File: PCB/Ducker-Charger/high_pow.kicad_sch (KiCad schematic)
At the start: 37 parts, among them Q1 NCE3080K, Q2 NCE3080K, Q3 NCE3080K, Q4 NCE3080K, Q5 NCE3080K, U1 BQ25713RSNR, U2 TPS25750DRJKR

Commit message: fix: Rshunt
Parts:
- removed Q1, Q2, Q3, Q4, Q5: NCE3080K, EasyEDA:TO-252-2_L6.6-W6.1-P4.57-LS9.9-TL-CW, symbol EasyEDA:NCE3080K
- added Q15, Q16, Q17, Q18, Q19: BSC040N08NS5, EasyEDA:PG-TDSON-8_L5.9-W5.1-P1.27-LS6.2-BL, symbol EasyEDA:BSC040N08NS5
- L1: value 10u -> 2.2u
- R2, R3: value 10m -> 5m; footprint (none) -> EasyEDA:R3920
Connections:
- net +BATT: now also Q15.1 (S), Q15.2 (S), Q15.3 (S)
- net ACN: now also Q19.5 (D), Q19.6 (D), Q19.7 (D), Q19.8 (D)
- net GND: now also Q17.1 (S), Q17.2 (S), Q17.3 (S), Q18.1 (S), Q18.2 (S), Q18.3 (S)
- net SW1: now also Q18.5 (D), Q18.6 (D), Q18.7 (D), Q18.8 (D), Q19.1 (S), Q19.2 (S), Q19.3 (S)
- net SW2: now also Q16.1 (S), Q16.2 (S), Q16.3 (S), Q17.5 (D), Q17.6 (D), Q17.7 (D), Q17.8 (D)
- net V_SYS_A: now also Q16.5 (D), Q16.6 (D), Q16.7 (D), Q16.8 (D)
- net V_SYS_B: now also Q15.5 (D), Q15.6 (D), Q15.7 (D), Q15.8 (D)
- net ~{BATDRV}: now also Q15.4 (G)
- net at R4.2: now also Q17.4 (G)
- net at R6.2: now also Q16.4 (G)
- net at R5.2: now also Q18.4 (G)
- net at R1.2: now also Q19.4 (G)
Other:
- note added: "50V"
- note added: "I_sat>20A"
- note added: "NB: Rshunt is now half the Datasheet"
- note removed: "30V"
- moved on the sheet: C5, R1, R4, R5, R6

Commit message: feat: updated footprints
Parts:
- C1, C6: footprint (none) -> Capacitor_SMD:CP_Elec_10x10
- C10, C4, C5, C9: footprint (none) -> Capacitor_SMD:C_0603_1608Metric
- C11, C12, C13, C14, C15: footprint (none) -> Capacitor_SMD:C_0805_2012Metric
- C2, C3, C7, C8: footprint (none) -> Capacitor_SMD:C_2220_5750Metric
- L1: footprint (none) -> Inductor_SMD:L_12x12mm_H6mm
- R1, R10, R11, R4, R5, R6, R7, R8, R9: footprint (none) -> Resistor_SMD:R_0603_1608Metric
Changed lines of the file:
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@@
 			)
 		)
-		(property "Footprint" ""
+		(property "Footprint" "Inductor_SMD:L_12x12mm_H6mm"
 			(at 165.1 60.96 0)
 			(effects
@@
 			)
 		)
-		(property "Footprint" ""
+		(property "Footprint" "Capacitor_SMD:C_0805_2012Metric"
 			(at 180.0352 139.7 0)
 			(effects
@@
 			)
 		)
-		(property "Footprint" ""
+		(property "Footprint" "Capacitor_SMD:C_2220_5750Metric"
 			(at 133.0452 73.66 0)
 			(effects
@@
 			)
 		)
-		(property "Footprint" ""
+		(property "Footprint" "Resistor_SMD:R_0603_1608Metric"
 			(at 155.448 46.99 90)
 			(effects
@@
 			)
 		)
-		(property "Footprint" ""
+		(property "Footprint" "Capacitor_SMD:C_2220_5750Metric"
 			(at 207.9752 73.66 0)
 			(effects
@@
 			)
 		)
-		(property "Footprint" ""
+		(property "Footprint" "Capacitor_SMD:CP_Elec_10x10"
 			(at 194.0052 73.66 0)
 			(effects
@@
 			)
 		)
-		(property "Footprint" ""
+		(property "Footprint" "Resistor_SMD:R_0603_1608Metric"
 			(at 177.038 86.36 90)
 			(effects
@@
 			)
 		)
-		(property "Footprint" ""
+		(property "Footprint" "Capacitor_SMD:C_0805_2012Metric"
 			(at 201.6252 139.7 0)
 			(effects
@@
 			)
 		)
-		(property "Footprint" ""
+		(property "Footprint" "Capacitor_SMD:C_2220_5750Metric"
 			(at 201.6252 73.66 0)
 			(effects
@@
 			)
 		)
-		(property "Footprint" ""
+		(property "Footprint" "Resistor_SMD:R_0603_1608Metric"
 			(at 179.578 46.99 90)
 			(effects
@@
 			)
 		)
-		(property "Footprint" ""
+		(property "Footprint" "Resistor_SMD:R_0603_1608Metric"
 			(at 159.258 86.36 90)
 			(effects
@@
 			)
 		)
-		(property "Footprint" ""
+		(property "Footprint" "Resistor_SMD:R_0603_1608Metric"
 			(at 103.632 143.51 90)
 			(effects
@@
 			)
 		)
-		(property "Footprint" ""
+		(property "Footprint" "Capacitor_SMD:C_0603_1608Metric"
 			(at 171.1452 139.7 0)
 			(effects
@@
 			)
 		)
-		(property "Footprint" ""
+		(property "Footprint" "Resistor_SMD:R_0603_1608Metric"
 			(at 103.632 135.89 90)
 			(effects
@@
 			)
 		)
-		(property "Footprint" ""
+		(property "Footprint" "Capacitor_SMD:C_0805_2012Metric"
 			(at 51.7652 185.42 0)
 			(effects
@@
 			)
 		)
-		(property "Footprint" ""
+		(property "Footprint" "Capacitor_SMD:C_0603_1608Metric"
 			(at 160.3248 48.26 0)
 			(effects
@@
 			)
 		)
-		(property "Footprint" ""
+		(property "Footprint" "Capacitor_SMD:CP_Elec_10x10"
 			(at 125.4252 73.66 0)
 			(effects
@@
 			)
 		)
-		(property "Footprint" ""
+		(property "Footprint" "Capacitor_SMD:C_2220_5750Metric"
 			(at 139.3952 73.66 0)
 			(effects
@@
 			)
 		)
-		(property "Footprint" ""
+		(property "Footprint" "Capacitor_SMD:C_0603_1608Metric"
 			(at 169.8752 55.88 0)
 			(effects
@@
 			)
 		)
-		(property "Footprint" ""
+		(property "Footprint" "Resistor_SMD:R_0603_1608Metric"
 			(at 196.85 133.858 90)
 			(effects
@@
 			)
 		)
-		(property "Footprint" ""
+		(property "Footprint" "Resistor_SMD:R_0603_1608Metric"
 			(at 129.032 135.89 90)
 			(effects
@@
 			)
 		)
-		(property "Footprint" ""
+		(property "Footprint" "Capacitor_SMD:C_0603_1608Metric"
 			(at 162.2552 139.7 0)
 			(effects
@@
 			)
 		)
-		(property "Footprint" ""
+		(property "Footprint" "Resistor_SMD:R_0603_1608Metric"
 			(at 129.032 143.51 90)
 			(effects
@@
 			)
 		)
-		(property "Footprint" ""
+		(property "Footprint" "Capacitor_SMD:C_0805_2012Metric"
 			(at 37.7952 185.42 0)
 			(effects
@@
 			)
 		)
-		(property "Footprint" ""
+		(property "Footprint" "Capacitor_SMD:C_0805_2012Metric"
 			(at 25.0952 185.42 0)
 			(effects

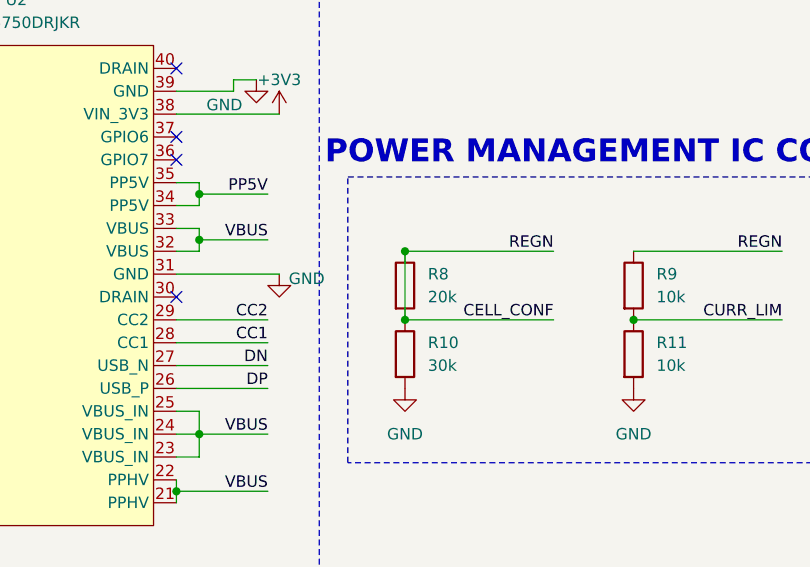
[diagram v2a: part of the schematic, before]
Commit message: fix: changed rshunt footprint
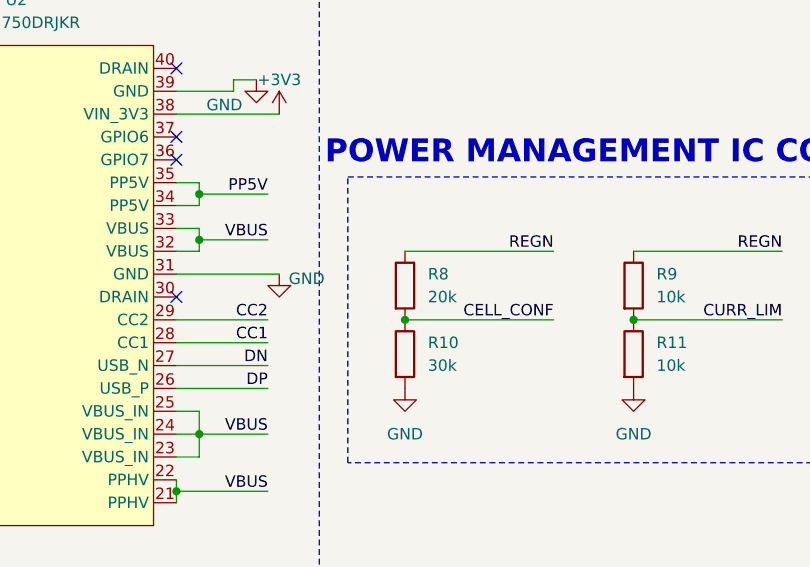
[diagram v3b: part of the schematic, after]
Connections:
- net CELL_CONF: no longer C11.1, R7.1, R8.1, R9.1, U1.28 (REGN)
- new net REGN: C11.1, R7.1, R8.1, R9.1, U1.28 (REGN)
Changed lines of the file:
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@@
-	)
-	(junction
-		(at 105.41 132.08)
-		(diameter 0)
-		(color 0 0 0 0)
 	)
 	(junction
@@
 		)
 		(stroke
-			(width 0)
-			(type default)
-		)
-	)
-	(wire
-		(pts
-			(xy 105.41 139.7) (xy 105.41 132.08)
-		)
-		(stroke

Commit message: fix: new BUCK-BOOST power stage
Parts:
- removed C10, C9: 100n, Capacitor_SMD:C_0603_1608Metric, symbol Device:C
- removed C11: 4.7u, Capacitor_SMD:C_0805_2012Metric, symbol Device:C
- removed C12: 1u, Capacitor_SMD:C_0805_2012Metric, symbol Device:C
- removed R10: 30k, Resistor_SMD:R_0603_1608Metric, symbol Device:R
- removed R11, R9: 10k, Resistor_SMD:R_0603_1608Metric, symbol Device:R
- removed R7: 10, Resistor_SMD:R_0603_1608Metric, symbol Device:R
- removed R8: 20k, Resistor_SMD:R_0603_1608Metric, symbol Device:R
- added C57, C77: 1u, symbol Device:C
- added C58, C59, C60, C61, C62, C63, C70, C71, C72, C73, C74, C75: 10u, symbol Device:C
- added C64: 470n, symbol Device:C
- added C65, C66: 33n, symbol Device:C
- added C67: 10n, symbol Device:C
- added C68, C69: 47n, symbol Device:C
- added C76: 0.1, symbol Device:C
- added L6: 2.2u, Inductor_SMD:L_12x12mm_H6mm, symbol Device:L
- added Q13, Q3, Q4, Q5: BSC040N08NS5, EasyEDA:PG-TDSON-8_L5.9-W5.1-P1.27-LS6.2-BL, symbol EasyEDA:BSC040N08NS5
- added Q14: PMOS, symbol Simulation_SPICE:PMOS
- added R58: 2.2, symbol Device:R
- added R59: 5m, EasyEDA:R3920, symbol Device:R
- added R60: 1, symbol Device:R
- added R61, R62: 4.99, symbol Device:R
- added R63: 10m, EasyEDA:R3920, symbol Device:R
- added R64, R65: 10, symbol Device:R
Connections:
- net +BATT: now also C76.1, R63.2, R65.1
- net ACN: now also C66.1, R62.2
- net ACP: now also C64.1, C65.1, R60.2, R61.2
- net BTST1: now also C68.2
- net BTST2: now also C69.2
- net GND: now also C57.2, C58.2, C59.2, C60.2, C61.2, C62.2, C63.2, C64.2, C65.2, C66.2, C67.2, C70.2, C71.2, C72.2, C73.2, C74.2, C75.2, C77.2, Q4.1 (S), Q4.2 (S), Q4.3 (S), Q5.1 (S), Q5.2 (S), Q5.3 (S)
- net HIDRV1: now also Q3.4 (G)
- net HIDRV2: now also Q13.4 (G)
- net LODRV1: now also Q4.4 (G)
- net LODRV2: now also Q5.4 (G)
- net SW1: now also C68.1, L6.1, Q3.1 (S), Q3.2 (S), Q3.3 (S), Q4.5 (D), Q4.6 (D), Q4.7 (D), Q4.8 (D)
- net SW2: now also C69.1, L6.2, Q13.5 (D), Q13.6 (D), Q13.7 (D), Q13.8 (D), Q5.5 (D), Q5.6 (D), Q5.7 (D), Q5.8 (D)
- net ~{BATDRV}: now also Q14.2 (G)
- new net: C76.2, C77.1, Q14.1 (D), R63.1, R64.1
- new net: C67.1, Q3.5 (D), Q3.6 (D), Q3.7 (D), Q3.8 (D), R59.2, R62.1
- new net: C57.1, R58.2
- new net ADAPTER: C58.1, C59.1, C60.1, C61.1, C62.1, C63.1, R58.1, R59.1, R60.1, R61.1
- new net SRN: R65.2
- new net SRP: R64.2
- new net SYS: C70.1, C71.1, C72.1, C73.1, C74.1, C75.1, Q13.1 (S), Q13.2 (S), Q13.3 (S), Q14.3 (S)
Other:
- note removed: "NB: Rshunt is now half the Datasheet"
- moved on the sheet: C1, C2, C3, C4, C5, C6, C7, C8, D2, D4, L1, Q15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

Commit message: fix: remade entire ICs configuration
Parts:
- removed C1: 220u, Capacitor_SMD:CP_Elec_10x10, symbol Device:C_Polarized
- removed C4, C5: 47n, Capacitor_SMD:C_0603_1608Metric, symbol Device:C
- removed D4: SMBJ22A-E3/52, EasyEDA:SMB_L4.3-W3.6-LS5.4-RD, symbol Device:D_Schottky
- removed L1: 2.2u, Inductor_SMD:L_12x12mm_H6mm, symbol Device:L
- removed Q14: PMOS, symbol Simulation_SPICE:PMOS
- removed Q15, Q16, Q17, Q18, Q19: BSC040N08NS5, EasyEDA:PG-TDSON-8_L5.9-W5.1-P1.27-LS6.2-BL, symbol EasyEDA:BSC040N08NS5
- removed R1, R4, R5, R6: 10, Resistor_SMD:R_0603_1608Metric, symbol Device:R
- removed R2, R3: 5m, EasyEDA:R3920, symbol Device:R
- added C1: 10u, symbol Device:C
- added C10: C, symbol Device:C
- added C11: 15p, symbol Device:C
- added C12: 1800p, symbol Device:C
- added C4, C5: 100u, symbol Device:C_Polarized
- added C78: 33p, symbol Device:C
- added C79: 680p, symbol Device:C
- added C80: 100p, symbol Device:C
- added C81: 10u, Capacitor_SMD:C_0603_1608Metric, symbol Device:C
- added C82: 330p, symbol Device:C
- added C9: 1u, symbol Device:C
- added D1: LED, LED_SMD:LED_0603_1608Metric, symbol Device:LED
- added Q15: SI7157DP-T1-GE3, EasyEDA:POWERPAK-SO-8_L5.9-W4.9-P1.27-LS6.2-BL, symbol EasyEDA:SI7157DP-T1-GE3
- added R10: 350k, Resistor_SMD:R_0603_1608Metric, symbol Device:R
- added R11: 250k, Resistor_SMD:R_0603_1608Metric, symbol Device:R
- added R66, R69, R74, R75: 10k, Resistor_SMD:R_0603_1608Metric, symbol Device:R
- added R67: 40.2k, Resistor_SMD:R_0603_1608Metric, symbol Device:R
- added R68: 137k, Resistor_SMD:R_0603_1608Metric, symbol Device:R
- added R7: 10, symbol Device:R
- added R70: 30k, Resistor_SMD:R_0603_1608Metric, symbol Device:R
- added R71: 100k, Resistor_SMD:R_0603_1608Metric, symbol Device:R
- added R72: 300k, Resistor_SMD:R_0603_1608Metric, symbol Device:R
- added R73: 1k, Resistor_SMD:R_0603_1608Metric, symbol Device:R
- added R8: 383k, Resistor_SMD:R_0603_1608Metric, symbol Device:R
- added R9: 220k, Resistor_SMD:R_0603_1608Metric, symbol Device:R
- C13, C14, C15: value 4.7u -> 10u
- C2, C3: footprint Capacitor_SMD:C_2220_5750Metric -> (none)
- C58, C59, C60, C61, C62, C63, C67, C70, C71, C72, C73, C74, C75: footprint (none) -> Capacitor_SMD:C_0603_1608Metric
- C6: value 220u -> 100u; footprint Capacitor_SMD:CP_Elec_10x10 -> (none)
- C7: value 22u -> 10u; footprint Capacitor_SMD:C_2220_5750Metric -> (none)
- C8: value 22u -> 330p; footprint Capacitor_SMD:C_2220_5750Metric -> (none)
- R59: value 5m -> 10m
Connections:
- net V_SYS_B is gone; now on net SRN: U1.19 (SRN)
- net +3V3: now also C6.1, C7.1, U2.34 (PP5V), U2.35 (PP5V), C4.1, C5.1, C81.1, R69.1
- net ACN: no longer C6.1, C7.1, C8.1
- net ACP: no longer C64.1, R60.2, U1.1 (VBUS), U2.20 (PPHV), U2.21 (PPHV), U2.22 (PPHV), U2.23 (VBUS_IN), U2.24 (VBUS_IN), U2.25 (VBUS_IN), U2.32 (VBUS), U2.33 (VBUS), USBC1.A4B9 (VBUS), USBC1.B4A9 (VBUS)
- net CC1: now also C8.1
- net CC2: now also C82.1
- net CELL_CONF: now also R71.2, R72.1
- net GND: now also U1.14 (CMPIN), U2.13 (GPIO11), U2.19 (GPIO3), U2.36 (GPIO7), U2.37 (GPIO6), U2.6 (GPIO1), U2.7 (GPIO2), C1.2, C10.2, C11.2, C12.2, C4.2, C5.2, C78.2, C79.2, C80.2, C81.2, C82.2, C9.2, D1.1 (K), R11.2, R68.2, R70.2, R72.2, R9.1
- net I2C_PD.SCL: no longer U1.13 (SCL)
- net I2C_PD.SDA: no longer U1.12 (SDA)
- net LDO_3V3: now also R74.1, R75.1
- net PP5V: no longer U2.34 (PP5V), U2.35 (PP5V)
- net REGN: now also C10.1, R7.1, R71.1
- net SRP: now also U1.20 (SRP)
- net SW2: now also Q13.1 (S), Q13.2 (S), Q13.3 (S); no longer Q13.5 (D), Q13.6 (D), Q13.7 (D), Q13.8 (D)
- net VDDA: now also C9.1, R10.1, R7.2, R8.2
- net ~{BATDRV}: now also Q15.4 (G)
- net at C76.2, C77.1, R63.1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: now also Q15.5 (D), Q15.6 (D), Q15.7 (D), Q15.8 (D)
- net PSYS: now reaches U1.10 (PSYS)
- net PSYS: now also R70.1
- net COMP1: now reaches U1.16 (COMP1)
- net COMP1: now also C78.1, R67.1
- net COMP2: now reaches U1.17 (COMP2)
- net COMP2: now also C11.1, R66.1
- net CHRG_OK: now reaches U1.4 (CHRG_OK)
- net CHRG_OK: now also R69.2
- net EN_OTG: now reaches U1.5 (OTG/VAP)
- net IADPT: now reaches U1.8 (IADPT)
- net IADPT: now also C80.1, R68.1
- net IBAT: now reaches U1.9 (IBAT)
- net V_WIRE: now reaches U2.15 (DRAIN)
- net V_WIRE: now also D2.5, U2.23 (VBUS_IN), U2.24 (VBUS_IN), U2.25 (VBUS_IN), U2.30 (DRAIN), U2.32 (VBUS), U2.33 (VBUS), U2.40 (DRAIN), USBC1.A4B9 (VBUS), USBC1.B4A9 (VBUS)
- net I2C_EX.SDA: now reaches U2.16 (I2Cm_SDA)
- net I2C_EX.SDA: now also U1.12 (SDA), R74.2
- net I2C_EX.SCL: now reaches U2.17 (I2Cm_SCL)
- net I2C_EX.SCL: now also U1.13 (SCL), R75.2
- net TPS_STATUS: now reaches U2.5 (GPIO0)
- net TPS_STATUS: now also R73.1
- net ADAPTER renamed 2USB
- net 2USB: now also C2.1, C3.1, U2.20 (PPHV), U2.21 (PPHV), U2.22 (PPHV), C1.1
- net DN renamed D-
- net DP renamed D+
- net SYS renamed VSYS
- net VSYS: now also Q13.5 (D), Q13.6 (D), Q13.7 (D), Q13.8 (D), U1.22 (VSYS), Q15.1 (S), Q15.2 (S), Q15.3 (S); no longer Q13.1 (S), Q13.2 (S), Q13.3 (S)
- removed net V_SYS_A: C2.1, C3.1, U1.20 (SRP), U1.22 (VSYS)
- new net: D1.2 (A), R73.2
- new net: C79.1, R66.2
- new net: C12.1, R67.2
- new net CELL_BATPRESZ: R10.2, R11.1
- new net ILIM_HIZ: R8.1, R9.2
- new net VBUS: C64.1, R60.2, U1.1 (VBUS)
- no-connect marks 11 -> 3
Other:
- note added: "/* ========================================================================== BQ25713 PINOUT REFERENCE & FUNCTIONAL GROUPS ========================================================================== */ /* -------------------------------------------------------------------------- 1. POWER PATH & SWITCHING (High Current / High Voltage) ----------------------------------------------------------------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"
- note added: "2.2-3.3u"
- note added: "ADC INPUT"
- note added: "BQ"
- note added: "CHIAVE"
- note added: "MCU"
- note added: "NOTE: CELL_BATPRESZ/CELL_CONF CONFIGURATION --------------------------------- Current Config: 4S (16.8V) R_high (to REGN): 100k (1%) R_low (to GND) : 300k (1%) Ratio = 300k / (100k + 300k) = 0.75 (75%) DATASHEET REFERENCE (Table 9-1) --------------------------------------------- | Cell | Pin Voltage | Charge V | SYSOVP | | Count| (% of VDDA) | Limit | Threshold | |------|-------------|----------|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"
- note added: "SVEGLIA"
- note added: "Status LED"
- note added: "UNUSED GPIO MUST BE GND TIED"
- note added: "VANNO A STM"
- note removed: "50V"
- note removed: "I_sat>20A"
- note removed: "Rshunt"
- moved on the sheet: C13, C14, C15, C57, C58, C59, C60, C61, C62, C63, C64, C65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
